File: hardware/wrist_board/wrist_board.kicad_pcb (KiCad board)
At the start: 4 copper layers, 60.7 x 45.1 mm, 63 parts, among them J1 S2B-PH-K-S_LF__SN_, J2 USB_C_Receptacle_USB2.0_14P, J3 Conn_01x02, J4 Conn_01x02, J5 Conn_01x02, J6 Conn_01x02, J7 Conn_01x02, J8 GPIOs, SW1 SW_SPST, SW2 BOOT_BTN, SW3 RST_BTN, U1 BQ24075RGT, U2 TLV75533PDBV, U3 MPU-6050, X1 ESP32-S3-WROOM-1-N16R8

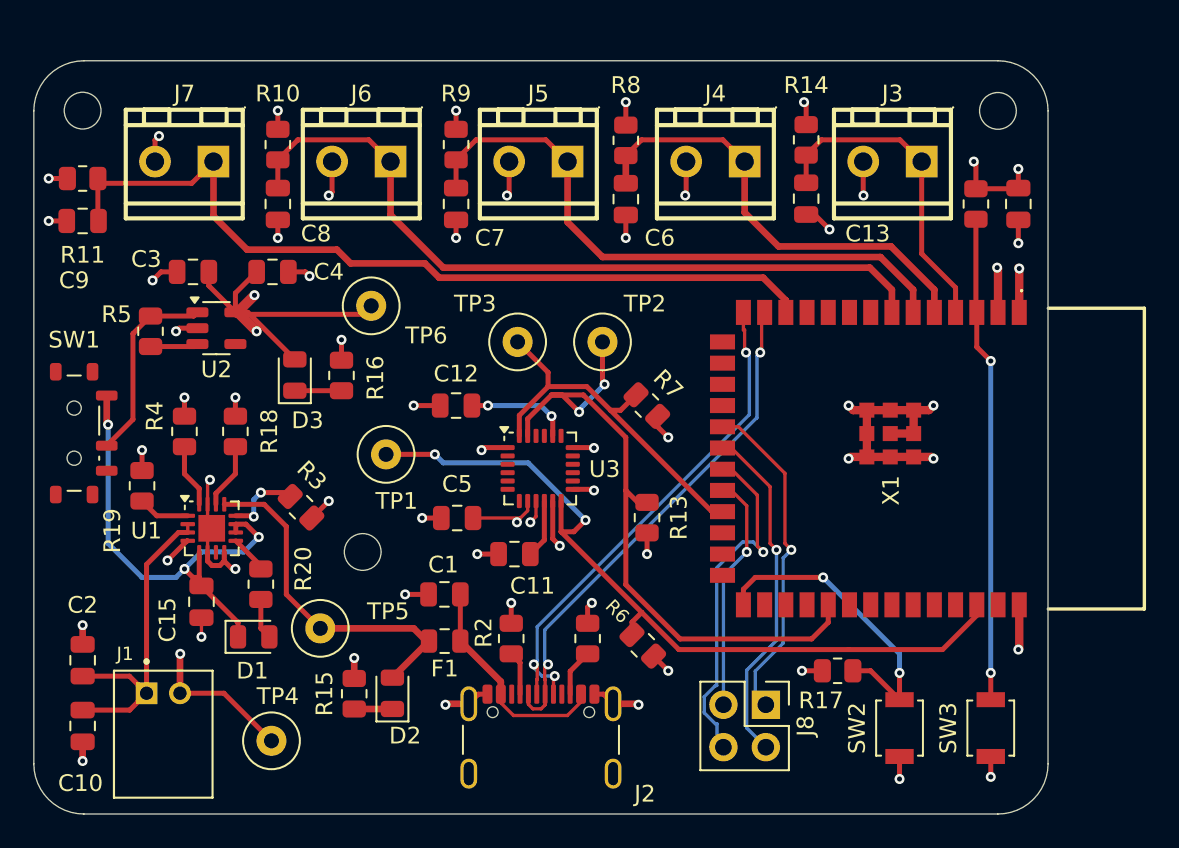
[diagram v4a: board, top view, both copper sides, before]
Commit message: Created processing board proj files, added usb c connectors
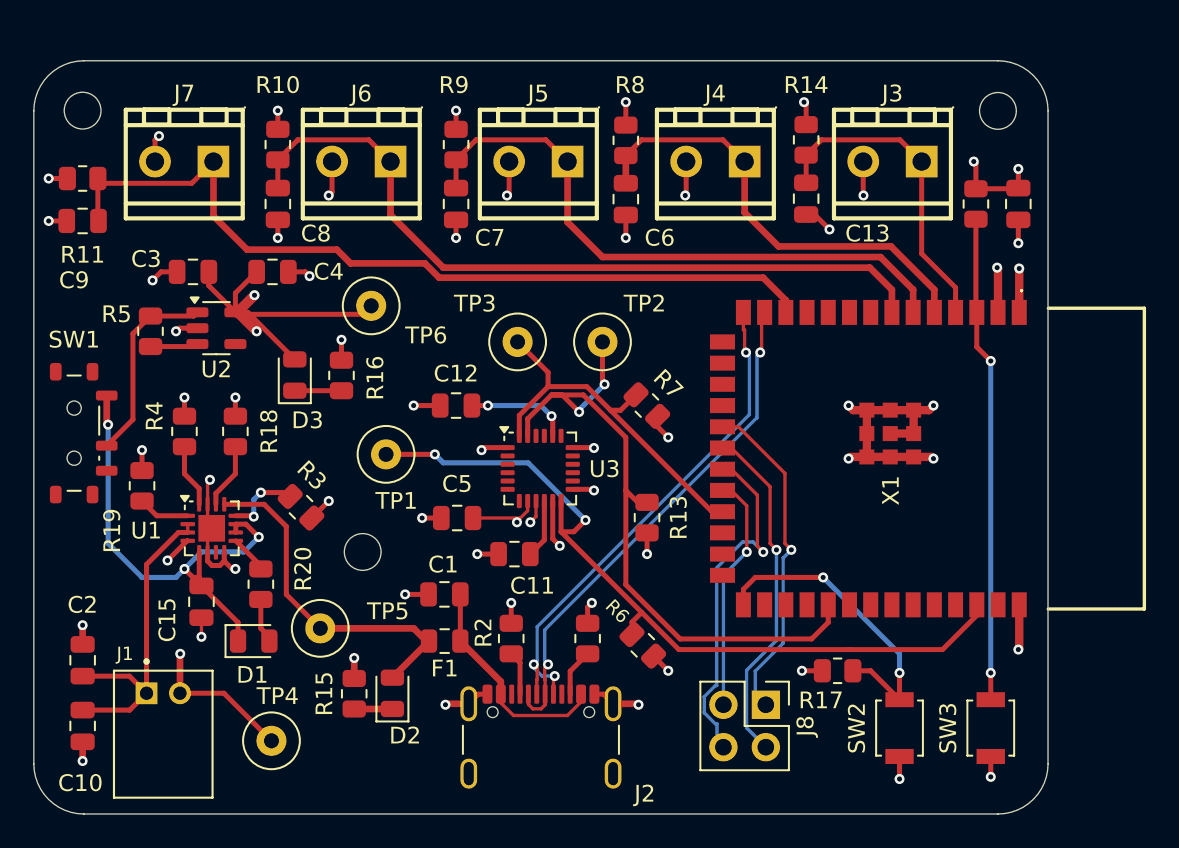
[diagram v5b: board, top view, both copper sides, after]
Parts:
- C12: value 0.1uF -> 2.2nF
- moved D1 0.25 mm to (79.3, 117.6)
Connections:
- D1 pad 1: /SYS -> Net-(D1-K)
- R20 pad 1: Net-(U1-~{CHG}) -> Net-(D1-A)
- R20 pad 2: Net-(D1-A) -> /SYS
- U1 pad 9: Net-(U1-~{CHG}) -> Net-(D1-K)
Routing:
- net Net-(U1-~{CHG}): track 2.30 -> 0.00 mm
- net Net-(D1-A): track 2.45 -> 4.75 mm
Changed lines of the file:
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@@
 	(net 64 "unconnected-(X1-IO16-Pad9)")
 	(net 65 "/SYS")
-	(net 66 "Net-(U1-~{CHG})")
+	(net 66 "Net-(D1-K)")
 	(net 67 "Net-(U1-ISET)")
 	(net 68 "unconnected-(U1-~{PGOOD}-Pad7)")
@@
 			)
 		)
-		(property "LCSC" "C15850"
+		(property "LCSC" "C1713"
 			(at 0 0 90)
 			(layer "F.SilkS")
@@
 		(tags "resistor")
 		(property "Reference" "R9"
-			(at 3.048 0 0)
+			(at 3.556 -0.127 0)
 			(layer "F.SilkS")
 			(effects
@@
 	(footprint "LED_SMD:LED_0805_2012Metric"
 		(layer "F.Cu")
-		(at 79.3265 117.348)
+		(at 79.3265 117.602)
 		(descr "LED SMD 0805 (2012 Metric), square (rectangular) end terminal, IPC-7351 nominal, (Body size source: https://docs.google.com/spreadsheets/d/1BsfQQcO9C6DZCsRaXUlFlo91Tg2WpOkGARC1WS5S8t0/edit?usp=sharing), generated with kicad-footprint-generator")
 		(tags "LED")
@@
 			)
 		)
+		(property "LCSC" "C2297"
+			(at 0 0 0)
+			(layer "F.SilkS")
+			(hide yes)
+			(effects
+				(font
+					(size 1.27 1.27)
+					(thickness 0.15)
+				)
+			)
+		)
 		(property ki_fp_filters "LED* LED_SMD:* LED_THT:*")
 		(sheetname "/")
@@
 			(layers "F.Cu" "F.Mask" "F.Paste")
 			(roundrect_rratio 0.25)
-			(net 65 "/SYS")
+			(net 66 "Net-(D1-K)")
 			(pinfunction "K")
 			(pintype "passive")
@@
 			)
 		)
+		(property "LCSC" "C1713"
+			(at 0 0 0)
+			(layer "F.SilkS")
+			(hide yes)
+			(effects
+				(font
+					(size 1.27 1.27)
+					(thickness 0.15)
+				)
+			)
+		)
 		(property ki_fp_filters "C_*")
 		(sheetname "/")
@@
 			)
 		)
+		(property "LCSC" "C17713"
+			(at 0 0 0)
+			(layer "F.SilkS")
+			(hide yes)
+			(effects
+				(font
+					(size 1.27 1.27)
+					(thickness 0.15)
+				)
+			)
+		)
 		(attr exclude_from_pos_files exclude_from_bom)
 		(fp_circle
@@
 			)
 		)
+		(property "LCSC" "C17713"
+			(at 0 0 0)
+			(layer "F.SilkS")
+			(hide yes)
+			(effects
+				(font
+					(size 1.27 1.27)
+					(thickness 0.15)
+				)
+			)
+		)
 		(property ki_fp_filters "R_*")
 		(sheetname "/")
@@
 		(tags "resistor")
 		(property "Reference" "R8"
-			(at 3.302 0 180)
+			(at 3.302 0.254 180)
 			(layer "F.SilkS")
 			(effects
@@
 			)
 		)
-		(property "LCSC" "C17414"
+		(property "LCSC" "C17513"
 			(at 0 0 90)
 			(layer "F.SilkS")
@@
 			)
 		)
+		(property "LCSC" "C17513"
+			(at 0 0 0)
+			(layer "F.SilkS")
+			(hide yes)
+			(effects
+				(font
+					(size 1.27 1.27)
+					(thickness 0.15)
+				)
+			)
+		)
 		(property ki_fp_filters "R_*")
 		(sheetname "/")
@@
 			(layers "F.Cu" "F.Mask" "F.Paste")
 			(roundrect_rratio 0.243902)
-			(net 66 "Net-(U1-~{CHG})")
+			(net 72 "Net-(D1-A)")
 			(pintype "passive")
 		)
@@
 			(layers "F.Cu" "F.Mask" "F.Paste")
 			(roundrect_rratio 0.243902)
-			(net 72 "Net-(D1-A)")
+			(net 65 "/SYS")
 			(pintype "passive")
 		)
@@
 			)
 		)
-		(property "LCSC" "C17414"
+		(property "LCSC" "C17513"
 			(at 0 0 0)
 			(layer "F.SilkS")
@@
 			)
 		)
-		(property "LCSC" "C15850"
+		(property "LCSC" "C1713"
 			(at 0 0 0)
 			(layer "F.SilkS")
@@
 			)
 		)
+		(property "LCSC" "C17414"
+			(at 0 0 0)
+			(layer "F.SilkS")
+			(hide yes)
+			(effects
+				(font
+					(size 1.27 1.27)
+					(thickness 0.15)
+				)
+			)
+		)
 		(property ki_fp_filters "R_*")
 		(sheetname "/")
@@
 			)
 		)
+		(property "LCSC" "C17398"
+			(at 0 0 0)
+			(layer "F.SilkS")
+			(hide yes)
+			(effects
+				(font
+					(size 1.27 1.27)
+					(thickness 0.15)
+				)
+			)
+		)
 		(property ki_fp_filters "R_*")
 		(sheetname "/")
@@
 			)
 		)
+		(property "LCSC" "C4310"
+			(at 0 0 0)
+			(layer "F.SilkS")
+			(hide yes)
+			(effects
+				(font
+					(size 1.27 1.27)
+					(thickness 0.15)
+				)
+			)
+		)
 		(property ki_fp_filters "R_*")
 		(sheetname "/")
@@
 			)
 		)
-		(property "Value" "0.1uF"
+		(property "Value" "2.2nF"
 			(at 0 1.68 0)
 			(layer "F.Fab")
@@
 		(tags "resistor")
 		(property "Reference" "R10"
-			(at 3.048 0 180)
+			(at 3.556 0 180)
 			(layer "F.SilkS")
 			(effects
@@
 			)
 		)
+		(property "LCSC" "C15464"
+			(at 0 0 0)
+			(layer "F.SilkS")
+			(hide yes)
+			(effects
+				(font
+					(size 1.27 1.27)
+					(thickness 0.15)
+				)
+			)
+		)
 		(property ki_fp_filters "VQFN*1EP*3x3mm*P0.5mm*")
 		(sheetname "/")
@@
 			(layers "F.Cu" "F.Mask" "F.Paste")
 			(roundrect_rratio 0.25)
-			(net 66 "Net-(U1-~{CHG})")
+			(net 66 "Net-(D1-K)")
 			(pinfunction "~{CHG}")
 			(pintype "open_collector")
@@
 	)
 	(segment
-		(start 79.756 113.1045)
-		(end 79.756 113.284)
-		(width 0.2)
-		(layer "F.Cu")
-		(net 66)
-	)
-	(segment
-		(start 78.2535 111.602)
-		(end 79.756 113.1045)
-		(width 0.3)
-		(layer "F.Cu")
-		(net 66)
-	)
-	(segment
 		(start 76.066 108.4745)
 		(end 75.184 107.5925)
@@
 		(width 0.3)
 		(layer "F.Cu")
+		(net 72)
+	)
+	(segment
+		(start 79.756 113.1045)
+		(end 79.756 113.284)
+		(width 0.2)
+		(layer "F.Cu")
+		(net 72)
+	)
+	(segment
+		(start 78.2535 111.602)
+		(end 79.756 113.1045)
+		(width 0.3)
+		(layer "F.Cu")
